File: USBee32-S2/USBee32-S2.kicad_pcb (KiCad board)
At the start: 4 copper layers, 28.1 x 68.3 mm, 46 parts, among them IC1 IP4220CZ6, J1 USB_A, J2 TYPE-C-31-M-12, J3 Conn_01x18_Male, J4 S2B-PH-SM4-TB(LF)(SN), J5 Conn_01x22_Male, Q1 MMBT8050, Q2 MMBT8050, SW1 SW_Push, SW2 SW_Push, U1 ESP32-S2-WROOM-ESP32-S2-WROOM, U2 MCP73831-2-OT, U3 AMS1117-3.3, U4 CH340C

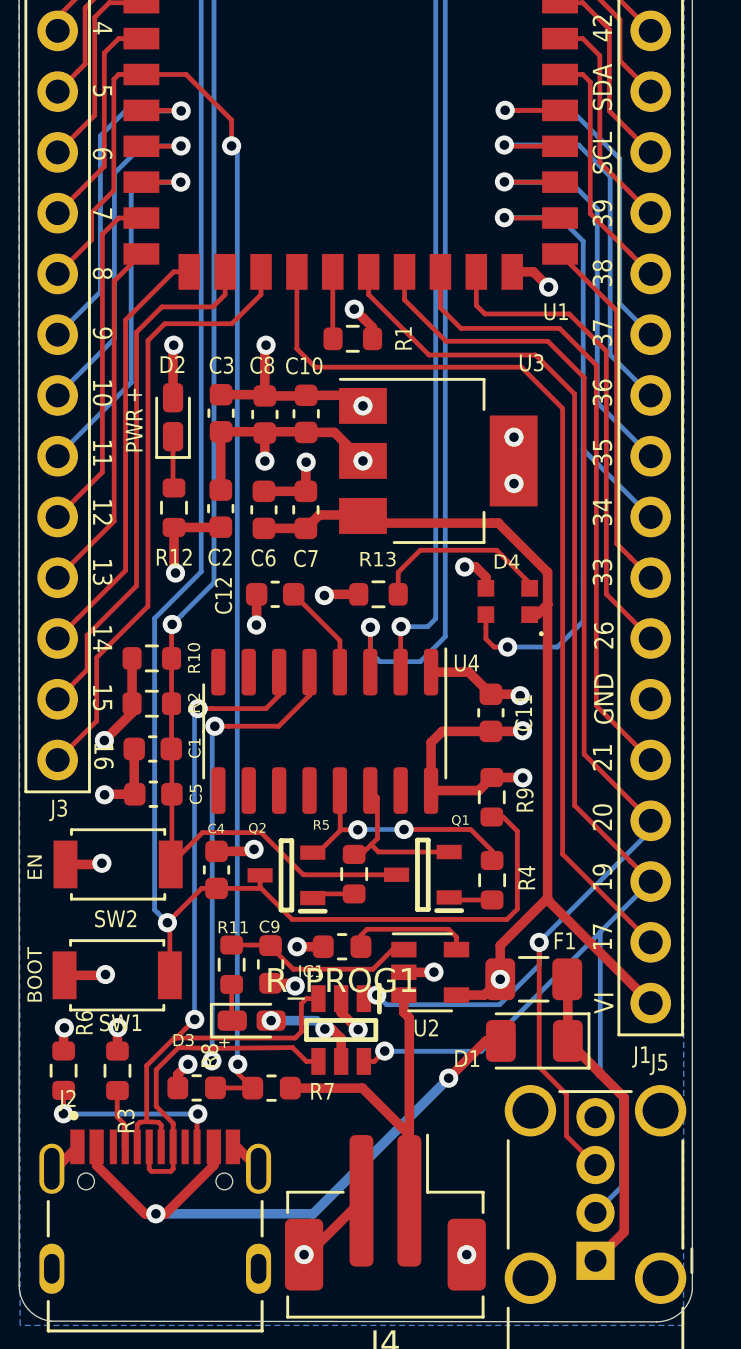
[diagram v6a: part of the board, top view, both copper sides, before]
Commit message: Updated routing, fixed issue with usb differential pair
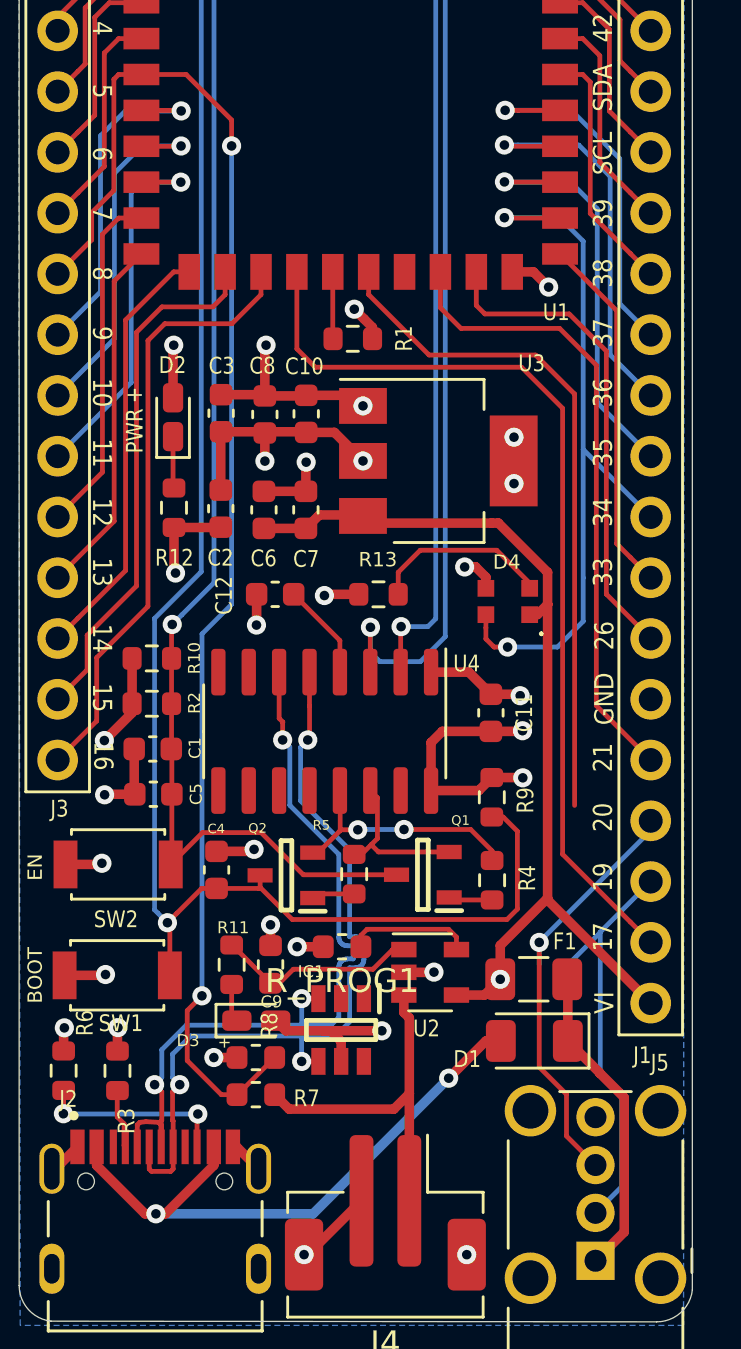
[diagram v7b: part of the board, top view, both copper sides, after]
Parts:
- moved R8 2.78 mm to (175.7, 113.6)
- moved R7 0.71 mm to (175.7, 115.2)
- moved D3 0.19 mm to (175.7, 112.1)
- turned C9 to 90 degrees
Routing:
- net /GPIO_20: track 56.2 -> 18.2 mm, vias 2 -> 1
- net /GPIO_19: track 60.7 -> 45.7 mm, vias 1 -> 0
- net +BATT: track 17.2 -> 14.8 mm
- net /VI: track 44.3 -> 46.5 mm, vias 3 -> 2
- net /GPIO_8: track 57.7 -> 59.9 mm
- net GND: track 58.2 -> 56.2 mm, vias 39 -> 38
- net /DP1: track 33.9 -> 33.3 mm, vias 2 -> 3
- net /DN1: track 33.1 -> 33.4 mm, vias 2 -> 3

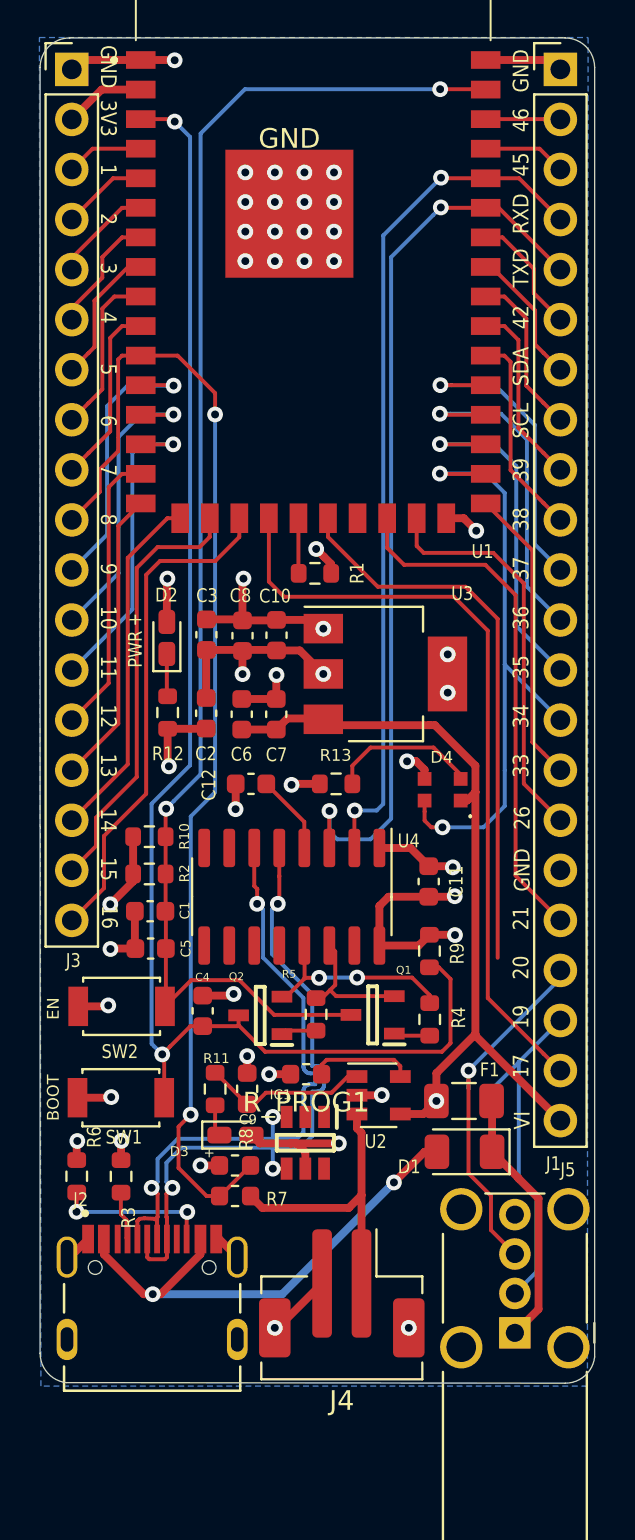
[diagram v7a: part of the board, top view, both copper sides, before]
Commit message: Completed routing 4-layer board
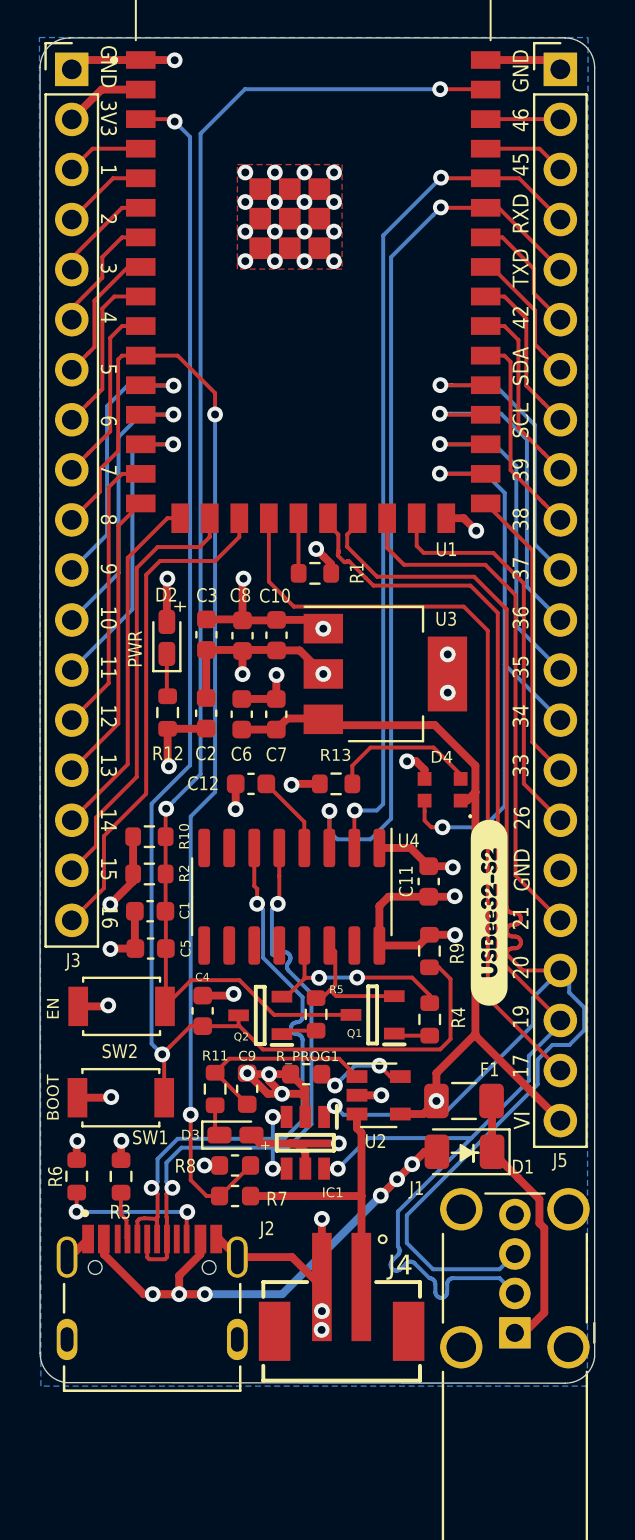
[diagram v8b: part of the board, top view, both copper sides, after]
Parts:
- removed GND: SolderWirePad_1x01_SMD_5x10mm, Connector_Wire:SolderWirePad_1x01_SMD_5x10mm
- added G***: LOGO, SRA_Logo:sralogo, B.Cu at (179.3, 71.7)
- added REF**: KiCad-Logo2_6mm_SilkScreen, Symbol:KiCad-Logo2_6mm_SilkScreen, B.Cu at (179.1, 100.5)
- added REF**: OSHW-Logo_5.7x6mm_SilkScreen, Designs:OSHW-Logo_5.7x6mm_SilkScreen, B.Cu at (178.6, 59.7)
- added svg2mod: G***, label, F.Cu at (188.6, 100.8)
- added svg2mod: G***, label, B.Cu at (179.6, 91.0)
- J4: value S2B-PH-SM4-TB(LF)(SN) -> B2B-PH-SM4-TB(LF)(SN); footprint Connector_JST:JST_PH_B2B-PH-SM4-TB_1x02-1MP_P2.00mm_Vertical -> B2B-PH-SM4-TB:JST_B2B-PH-SM4-TB(LF)(SN)
- moved J4 0.32 mm to (181.1, 119.8)
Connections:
- net /GPIO_19 renamed /D1-
- net /GPIO_20 renamed /D1+
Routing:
- net /D1+: track 18.2 -> 74.7 mm
- net /D1-: track 45.7 -> 66.5 mm, vias 0 -> 1
- net GND: track 56.2 -> 69.7 mm, vias 38 -> 40
- net /VBUSC: track 25.5 -> 29.6 mm, vias 2 -> 6
- net Net-(C9-Pad1): track 8.44 -> 10.5 mm
- net /DP1: track 33.3 -> 32.7 mm
- net /DN1: track 33.4 -> 32.7 mm
- net /VBUSA: track 13.2 -> 13.8 mm
- net /GPIO_8: track 59.9 -> 59.4 mm
- net Net-(R_PROG1-Pad1): track 5.23 -> 4.88 mm, vias 0 -> 2
- added copper zone on F.Cu, net GND
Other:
- board text added: "Society of Robotics and Automation"
- board text removed: "DESIGNED WITH"
